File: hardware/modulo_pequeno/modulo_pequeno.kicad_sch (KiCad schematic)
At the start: 18 parts, among them J1 Backplane (IDC 2x8), J2 Entradas 0-7, J3 LEDs 0-7, J4 Analógico (joystick, acelerad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, U1 74HC165, U2 74HC595

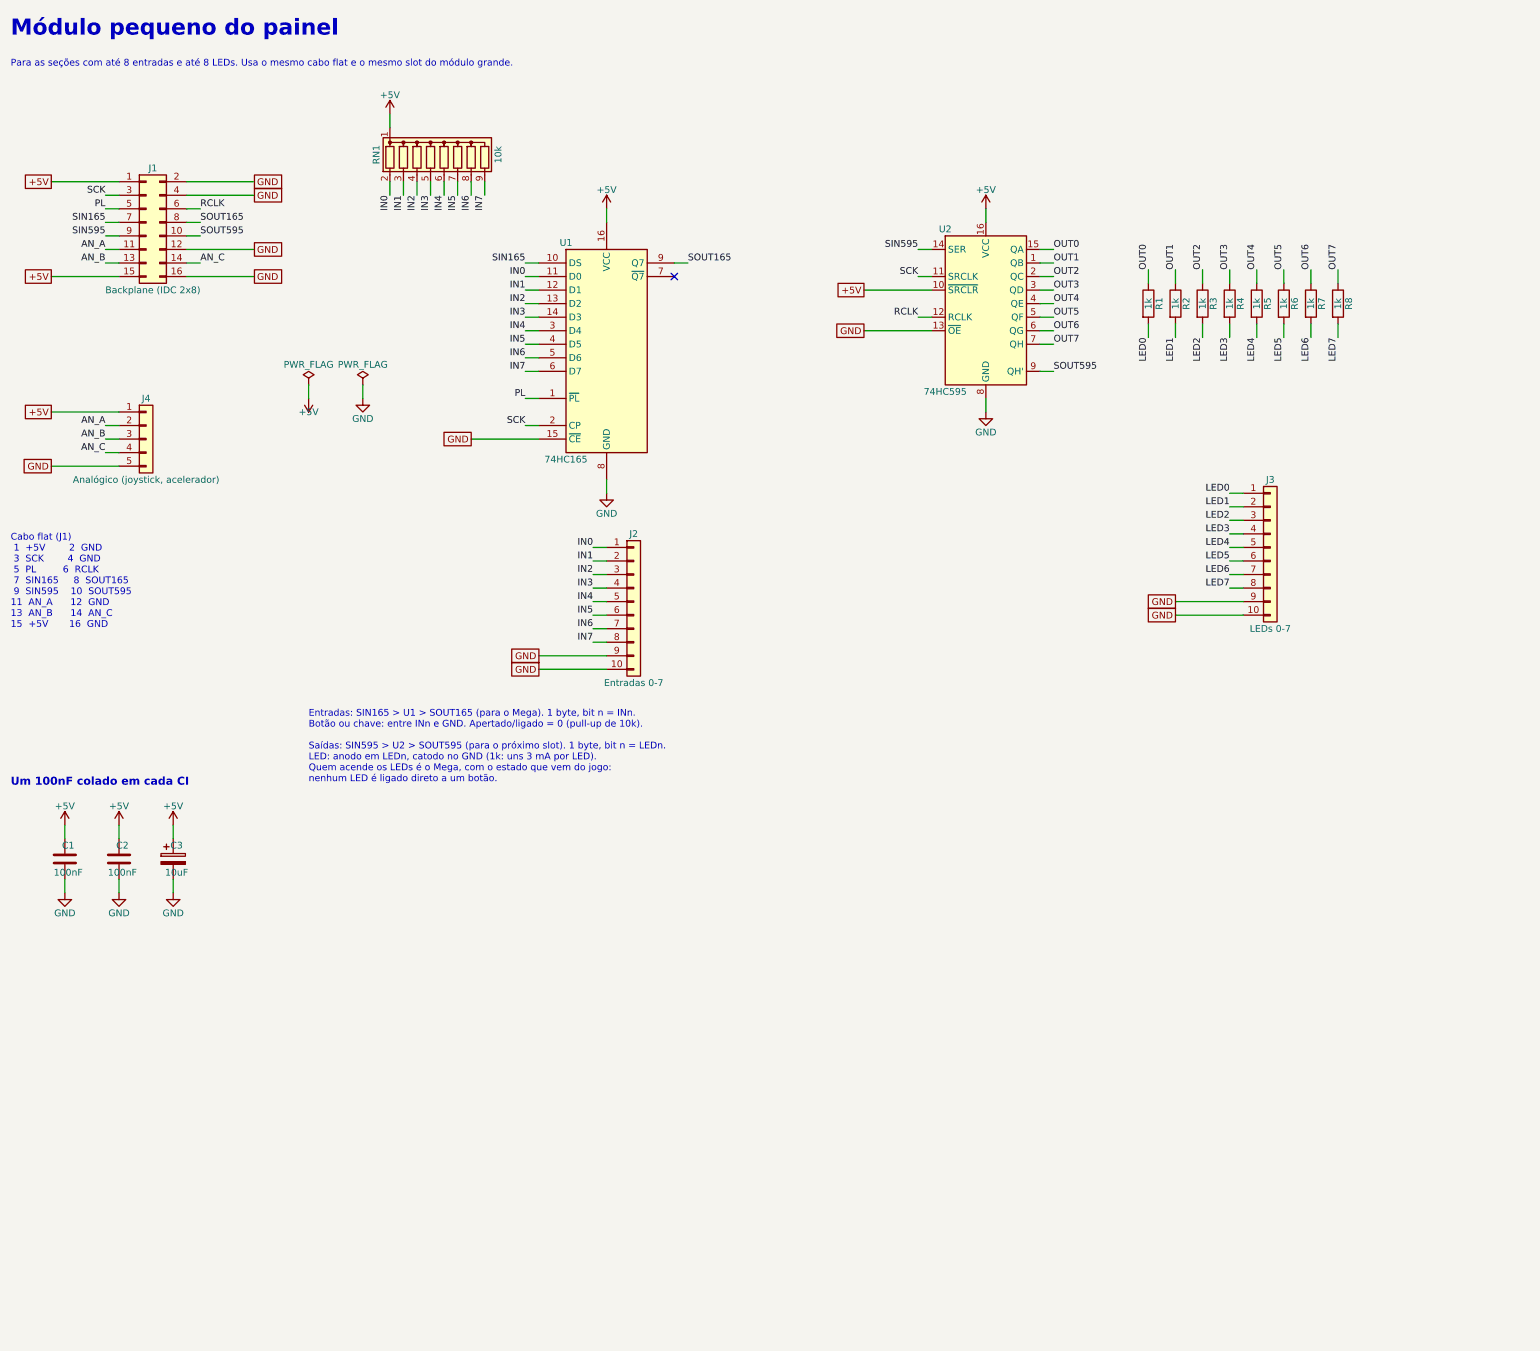
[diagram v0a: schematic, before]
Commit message: Hardware: etiqueta com chave DIP para o Mega reconhecer cada módulo
- Módulos pequeno, médio e grande: mais um 74HC165 (U1) ligado a uma
  chave DIP de 8 vias, como primeiro byte de cada módulo na cadeia.
  Bits 7-6 dizem o tamanho da placa e 5-0 o número da seção, então o
  Mega percorre a fila sozinho, sem tabela de slots no firmware
- Os três módulos agora saem de um gerador só, com a mesma numeração
- Backplane: pull-down também no MISO, para o Mega ler "fim da fila"
  mesmo sem nenhum módulo; nota de que a ordem dos módulos não importa
- hardware/README.md: etiqueta, números e chaves DIP sugeridos para cada
  seção, teste de um módulo direto no Mega com 8 fios, ordem dos bytes
  e lista de peças atualizadas
- README: etiqueta na decisão de arquitetura, fase 2 e lista de compras

Co-Authored-By: Claude Opus 5.5 <noreply@anthropic.com>
Claude-Session: https://claude.ai/code/session_01XMhb4PzDFxzjZohaF3KBWg
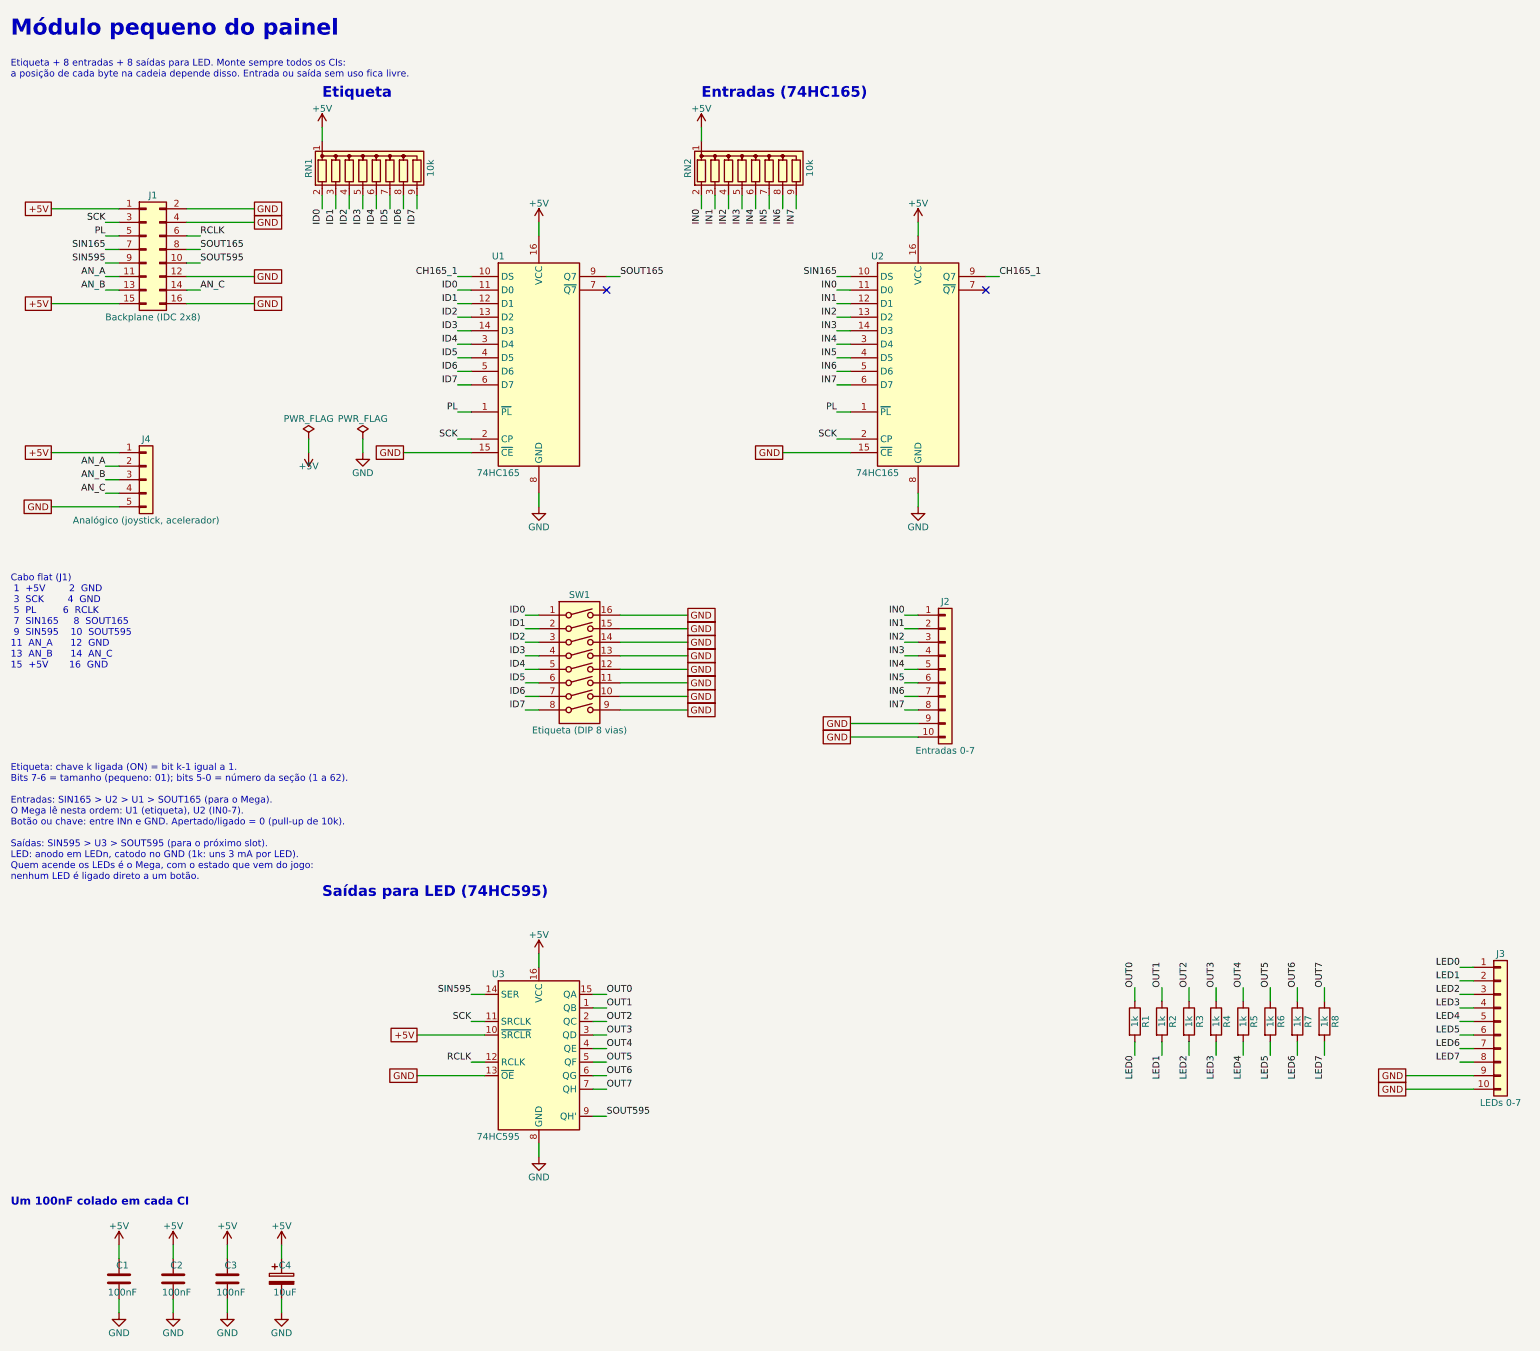
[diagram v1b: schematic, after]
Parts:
- removed C3: 10uF, Capacitor_THT:CP_Radial_D5.0mm_P2.00mm, symbol Device:C_Polarized
- removed U2: 74HC595, Package_DIP:DIP-16_W7.62mm_Socket, symbol 74xx:74HC595
- added C3: 100nF, Capacitor_THT:C_Disc_D5.0mm_W2.5mm_P5.00mm, symbol Device:C
- added C4: 10uF, Capacitor_THT:CP_Radial_D5.0mm_P2.00mm, symbol Device:C_Polarized
- added RN2: 10k, Resistor_THT:R_Array_SIP9, symbol Device:R_Network08
- added SW1: Etiqueta (DIP 8 vias), Button_Switch_THT:SW_DIP_SPSTx08_Slide_9.78x22.5mm_W7.62mm_P2.54mm, symbol Switch:SW_DIP_x08
- added U2: 74HC165, Package_DIP:DIP-16_W7.62mm_Socket, symbol 74xx:74HC165
- added U3: 74HC595, Package_DIP:DIP-16_W7.62mm_Socket, symbol 74xx:74HC595
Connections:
- net +5V: now also C3.1, C4.1, RN2.1 (common), U2.16 (VCC), U3.10 (~{SRCLR}), U3.16 (VCC)
- net GND: now also C3.2, C4.2, SW1.10, SW1.11, SW1.12, SW1.13, SW1.14, SW1.15, SW1.16, SW1.9, U2.15 (~{CE}), U2.8 (GND), U3.13 (~{OE}), U3.8 (GND)
- net IN0: now also RN2.2 (R1), U2.11 (D0); no longer RN1.2 (R1), U1.11 (D0)
- net IN1: now also RN2.3 (R2), U2.12 (D1); no longer RN1.3 (R2), U1.12 (D1)
- net IN2: now also RN2.4 (R3), U2.13 (D2); no longer RN1.4 (R3), U1.13 (D2)
- net IN3: now also RN2.5 (R4), U2.14 (D3); no longer RN1.5 (R4), U1.14 (D3)
- net IN4: now also RN2.6 (R5), U2.3 (D4); no longer RN1.6 (R5), U1.3 (D4)
- net IN5: now also RN2.7 (R6), U2.4 (D5); no longer RN1.7 (R6), U1.4 (D5)
- net IN6: now also RN2.8 (R7), U2.5 (D6); no longer RN1.8 (R7), U1.5 (D6)
- net IN7: now also RN2.9 (R8), U2.6 (D7); no longer RN1.9 (R8), U1.6 (D7)
- net OUT0: now also U3.15 (QA)
- net OUT1: now also U3.1 (QB)
- net OUT2: now also U3.2 (QC)
- net OUT3: now also U3.3 (QD)
- net OUT4: now also U3.4 (QE)
- net OUT5: now also U3.5 (QF)
- net OUT6: now also U3.6 (QG)
- net OUT7: now also U3.7 (QH)
- net PL: now also U2.1 (~{PL})
- net RCLK: now also U3.12 (RCLK)
- net SCK: now also U2.2 (CP), U3.11 (SRCLK)
- net SIN165: now also U2.10 (DS); no longer U1.10 (DS)
- net SIN595: now also U3.14 (SER)
- net SOUT595: now also U3.9 (QH')
- new net CH165_1: U1.10 (DS), U2.9 (Q7)
- new net ID0: RN1.2 (R1), SW1.1, U1.11 (D0)
- new net ID1: RN1.3 (R2), SW1.2, U1.12 (D1)
- new net ID2: RN1.4 (R3), SW1.3, U1.13 (D2)
- new net ID3: RN1.5 (R4), SW1.4, U1.14 (D3)
- new net ID4: RN1.6 (R5), SW1.5, U1.3 (D4)
- new net ID5: RN1.7 (R6), SW1.6, U1.4 (D5)
- new net ID6: RN1.8 (R7), SW1.7, U1.5 (D6)
- new net ID7: RN1.9 (R8), SW1.8, U1.6 (D7)
- no-connect marks 1 -> 2
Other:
- note added: "Entradas (74HC165)"
- note added: "Etiqueta"
- note added: "Etiqueta + 8 entradas + 8 saídas para LED. Monte sempre todos os CIs: a posição de cada byte na cadeia depende disso. Entrada ou saída sem uso fica livre."
- note added: "Etiqueta: chave k ligada (ON) = bit k-1 igual a 1. Bits 7-6 = tamanho (pequeno: 01); bits 5-0 = número da seção (1 a 62). Entradas: SIN165 > U2 > U1 > SOUT165 (para o Mega). O Mega lê nesta ordem: U1 (etiqueta), U2 (IN0-7). Botão ou chave: entre INn e GND. Apertado/ligado = 0 (pull-up de 10k). Saídas: SIN595 > U3 > SOUT595 (para o próximo slot). LED: anodo em LEDn, catodo no GND (1k: uns 3 mA por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"
- note added: "Saídas para LED (74HC595)"
- note removed: "Entradas: SIN165 > U1 > SOUT165 (para o Mega). 1 byte, bit n = INn. Botão ou chave: entre INn e GND. Apertado/ligado = 0 (pull-up de 10k). Saídas: SIN595 > U2 > SOUT595 (para o próximo slot). 1 byte, bit n = LEDn. LED: anodo em LEDn, catodo no GND (1k: uns 3 mA por LED). Quem acende os LEDs é o Mega, com o estado que vem do jogo: nenhum LED é ligado direto a um botão."
- note removed: "Para as seções com até 8 entradas e até 8 LEDs. Usa o mesmo cabo flat e o mesmo slot do módulo grande."
